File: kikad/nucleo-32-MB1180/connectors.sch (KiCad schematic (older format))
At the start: 2 parts, among them J1 Conn_01x15, J2 Conn_01x15

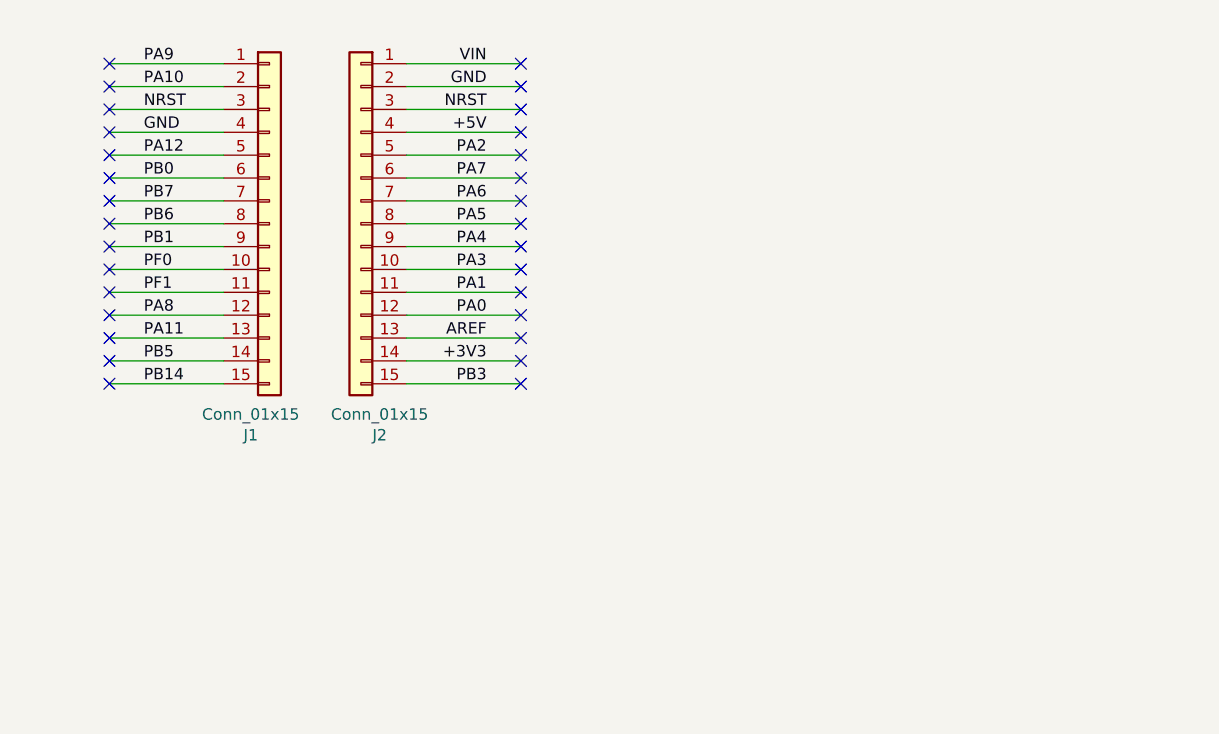
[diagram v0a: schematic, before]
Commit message: add nucleo-32-MB1180
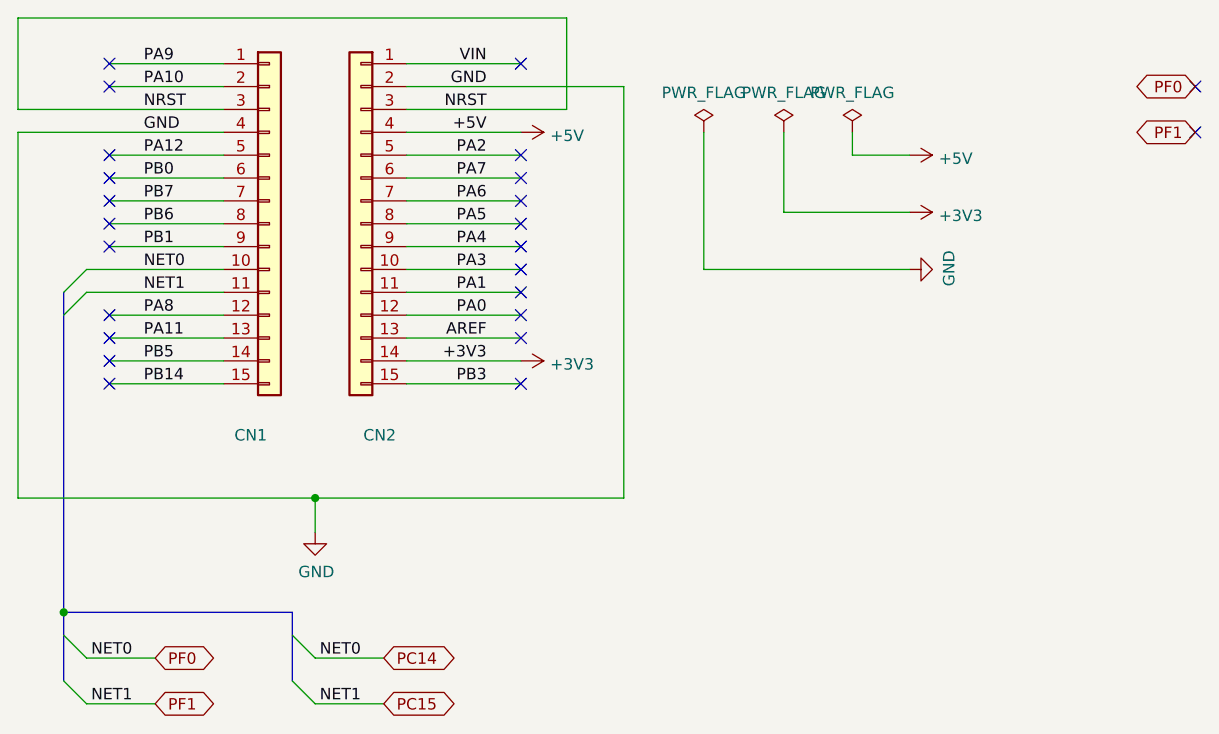
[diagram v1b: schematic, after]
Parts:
- renumbered J1 to CN1, J2 to CN2
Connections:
- net PF0 renamed PC14
- net PF1 renamed PC15
- no-connect marks 30 -> 24
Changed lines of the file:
@@
 $EndDescr
 $Comp
-L Connector_Generic:Conn_01x15 J2
+L Connector_Generic:Conn_01x15 CN2
 U 1 1 600C5B3D
 P 2300 1600
-F 0 "J2" H 2218 675 50  0000 C CNN
-F 1 "Conn_01x15" H 2218 766 50  0000 C CNN
+F 0 "CN2" H 2218 675 50  0000 C CNN
+F 1 "Conn_01x15" H 2218 766 50  0001 C CNN
 F 2 "Connector_PinSocket_2.54mm:PinSocket_1x15_P2.54mm_Vertical" H 2300 1600 50  0001 C CNN
 F 3 "~" H 2300 1600 50  0001 C CNN
@@
 	1200 2300 1700 2300
 $Comp
-L Connector_Generic:Conn_01x15 J1
+L Connector_Generic:Conn_01x15 CN1
 U 1 1 600C2485
 P 1900 1600
-F 0 "J1" H 1818 675 50  0000 C CNN
-F 1 "Conn_01x15" H 1818 766 50  0000 C CNN
+F 0 "CN1" H 1818 675 50  0000 C CNN
+F 1 "Conn_01x15" H 1818 766 50  0001 C CNN
 F 2 "Connector_PinSocket_2.54mm:PinSocket_1x15_P2.54mm_Vertical" H 1900 1600 50  0001 C CNN
 F 3 "~" H 1900 1600 50  0001 C CNN
@@
 	1200 2000 1700 2000
 Wire Wire Line
-	1200 1900 1700 1900
-Wire Wire Line
-	1200 1800 1700 1800
-Wire Wire Line
 	1200 1700 1700 1700
 Wire Wire Line
@@
 Wire Wire Line
 	1200 1300 1700 1300
-Wire Wire Line
-	1200 1200 1700 1200
-Wire Wire Line
-	1200 1100 1700 1100
 Wire Wire Line
 	1200 1000 1700 1000
@@
 NoConn ~ 1200 900
 NoConn ~ 1200 1000
-NoConn ~ 1200 1100
-NoConn ~ 1200 1200
 NoConn ~ 1200 1300
 NoConn ~ 1200 1400
@@
 NoConn ~ 1200 1600
 NoConn ~ 1200 1700
-NoConn ~ 1200 1800
-NoConn ~ 1200 1900
 NoConn ~ 1200 2000
 NoConn ~ 1200 2100
@@
 PA8
 Text Label 1350 1900 0    50   ~ 0
-PF1
+NET1
 Text Label 1350 1800 0    50   ~ 0
-PF0
+NET0
 Text Label 1350 1700 0    50   ~ 0
 PB1
@@
 PA9
 NoConn ~ 3000 900
-NoConn ~ 3000 1000
-NoConn ~ 3000 1100
-NoConn ~ 3000 1200
 NoConn ~ 3000 1300
 NoConn ~ 3000 1400
@@
 NoConn ~ 3000 2000
 NoConn ~ 3000 2100
-NoConn ~ 3000 2200
 NoConn ~ 3000 2300
 Text Label 2850 2000 2    50   ~ 0
@@
 	3000 900  2500 900
 Wire Wire Line
-	3000 1000 2500 1000
-Wire Wire Line
-	3000 1100 2500 1100
-Wire Wire Line
 	3000 1200 2500 1200
 Wire Wire Line
@@
 Wire Wire Line
 	3000 2300 2500 2300
+$Comp
+L power:+3V3 #PWR0101
+U 1 1 600FBD88
+P 3000 2200
+F 0 "#PWR0101" H 3000 2050 50  0001 C CNN
+F 1 "+3V3" V 3015 2328 50  0000 L CNN
+F 2 "" H 3000 2200 50  0001 C CNN
+F 3 "" H 3000 2200 50  0001 C CNN
+	1    3000 2200
+	0    1    1    0
+$EndComp
+$Comp
+L power:+5V #PWR0102
+U 1 1 60101FFD
+P 3000 1200
+F 0 "#PWR0102" H 3000 1050 50  0001 C CNN
+F 1 "+5V" V 3015 1328 50  0000 L CNN
+F 2 "" H 3000 1200 50  0001 C CNN
+F 3 "" H 3000 1200 50  0001 C CNN
+	1    3000 1200
+	0    1    1    0
+$EndComp
+$Comp
+L power:GND #PWR0103
+U 1 1 6010AA0D
+P 2100 2950
+F 0 "#PWR0103" H 2100 2700 50  0001 C CNN
+F 1 "GND" H 2105 2777 50  0000 C CNN
+F 2 "" H 2100 2950 50  0001 C CNN
+F 3 "" H 2100 2950 50  0001 C CNN
+	1    2100 2950
+	1    0    0    -1
+$EndComp
+Wire Wire Line
+	800  1200 800  2800
+Wire Wire Line
+	800  2800 2100 2800
+Wire Wire Line
+	3450 2800 3450 1000
+Wire Wire Line
+	800  1200 1700 1200
+Wire Wire Line
+	2500 1000 3450 1000
+Wire Wire Line
+	2100 2800 2100 2950
+Connection ~ 2100 2800
+Wire Wire Line
+	2100 2800 3450 2800
+$Comp
+L power:PWR_FLAG #FLG0101
+U 1 1 600C7F8E
+P 3800 1200
+F 0 "#FLG0101" H 3800 1275 50  0001 C CNN
+F 1 "PWR_FLAG" H 3800 1373 50  0000 C CNN
+F 2 "" H 3800 1200 50  0001 C CNN
+F 3 "~" H 3800 1200 50  0001 C CNN
+	1    3800 1200
+	1    0    0    -1
+$EndComp
+$Comp
+L power:PWR_FLAG #FLG0102
+U 1 1 600C8995
+P 4150 1200
+F 0 "#FLG0102" H 4150 1275 50  0001 C CNN
+F 1 "PWR_FLAG" H 4150 1373 50  0000 C CNN
+F 2 "" H 4150 1200 50  0001 C CNN
+F 3 "~" H 4150 1200 50  0001 C CNN
+	1    4150 1200
+	1    0    0    -1
+$EndComp
+$Comp
+L power:PWR_FLAG #FLG0103
+U 1 1 600C8E93
+P 4450 1200
+F 0 "#FLG0103" H 4450 1275 50  0001 C CNN
+F 1 "PWR_FLAG" H 4450 1373 50  0000 C CNN
+F 2 "" H 4450 1200 50  0001 C CNN
+F 3 "~" H 4450 1200 50  0001 C CNN
+	1    4450 1200
+	1    0    0    -1
+$EndComp
+$Comp
+L power:GND #PWR0104
+U 1 1 600C83B4
+P 4700 1800
+F 0 "#PWR0104" H 4700 1550 50  0001 C CNN
+F 1 "GND" H 4705 1627 50  0000 C CNN
+F 2 "" H 4700 1800 50  0001 C CNN
+F 3 "" H 4700 1800 50  0001 C CNN
+	1    4700 1800
+	0    -1   -1   0
+$EndComp
+$Comp
+L power:+3V3 #PWR0105
+U 1 1 600D0100
+P 4700 1550
+F 0 "#PWR0105" H 4700 1400 50  0001 C CNN
+F 1 "+3V3" V 4715 1678 50  0000 L CNN
+F 2 "" H 4700 1550 50  0001 C CNN
+F 3 "" H 4700 1550 50  0001 C CNN
+	1    4700 1550
+	0    1    1    0
+$EndComp
+$Comp
+L power:+5V #PWR0106
+U 1 1 600D0206
+P 4700 1300
+F 0 "#PWR0106" H 4700 1150 50  0001 C CNN
+F 1 "+5V" V 4715 1428 50  0000 L CNN
+F 2 "" H 4700 1300 50  0001 C CNN
+F 3 "" H 4700 1300 50  0001 C CNN
+	1    4700 1300
+	0    1    1    0
+$EndComp
+Wire Wire Line
+	4700 1800 3800 1800
+Wire Wire Line
+	3800 1200 3800 1800
+Wire Wire Line
+	4150 1200 4150 1550
+Wire Wire Line
+	4150 1550 4700 1550
+Wire Wire Line
+	4450 1200 4450 1300
+Wire Wire Line
+	4450 1300 4700 1300
+Wire Wire Line
+	800  1100 800  700
+Wire Wire Line
+	800  700  3200 700
+Wire Wire Line
+	3200 700  3200 1100
+Wire Wire Line
+	800  1100 1700 1100
+Wire Wire Line
+	2500 1100 3200 1100
+Entry Wire Line
+	1100 1800 1000 1900
+Entry Wire Line
+	1100 1900 1000 2000
+Text GLabel 1400 3500 2    50   BiDi ~ 0
+PF0
+Text GLabel 1400 3700 2    50   BiDi ~ 0
+PF1
+Entry Wire Line
+	1000 3400 1100 3500
+Entry Wire Line
+	1000 3600 1100 3700
+Wire Wire Line
+	1100 3500 1400 3500
+Wire Wire Line
+	1100 3700 1400 3700
+Text Label 1300 3500 2    50   ~ 0
+NET0
+Text Label 1300 3700 2    50   ~ 0
+NET1
+Text GLabel 5950 1000 0    50   BiDi ~ 0
+PF0
+Text GLabel 5950 1200 0    50   BiDi ~ 0
+PF1
+NoConn ~ 5950 1000
+NoConn ~ 5950 1200
+Text GLabel 2400 3500 2    50   BiDi ~ 0
+PC14
+Text GLabel 2400 3700 2    50   BiDi ~ 0
+PC15
+Entry Wire Line
+	2000 3400 2100 3500
+Entry Wire Line
+	2000 3600 2100 3700
+Wire Wire Line
+	2100 3500 2400 3500
+Wire Wire Line
+	2100 3700 2400 3700
+Text Label 2300 3500 2    50   ~ 0
+NET0
+Text Label 2300 3700 2    50   ~ 0
+NET1
+Wire Wire Line
+	1100 1800 1700 1800
+Wire Wire Line
+	1100 1900 1700 1900
+Wire Bus Line
+	2000 3300 1000 3300
+Wire Bus Line
+	2000 3300 2000 3600
+Wire Bus Line
+	1000 1900 1000 3300
+Connection ~ 1000 3300
+Wire Bus Line
+	1000 3300 1000 3600
 $EndSCHEMATC
